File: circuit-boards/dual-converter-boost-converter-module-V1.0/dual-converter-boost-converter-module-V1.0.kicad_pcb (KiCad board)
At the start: 4 copper layers, 70 x 34 mm, 39 parts, among them J1 Vout Conn, J2 Conn_01x06, J3 Vout Conn, U1 TPL0401B-10DCKR, U2 LM5156HPWPR, U3 STN3N40K3

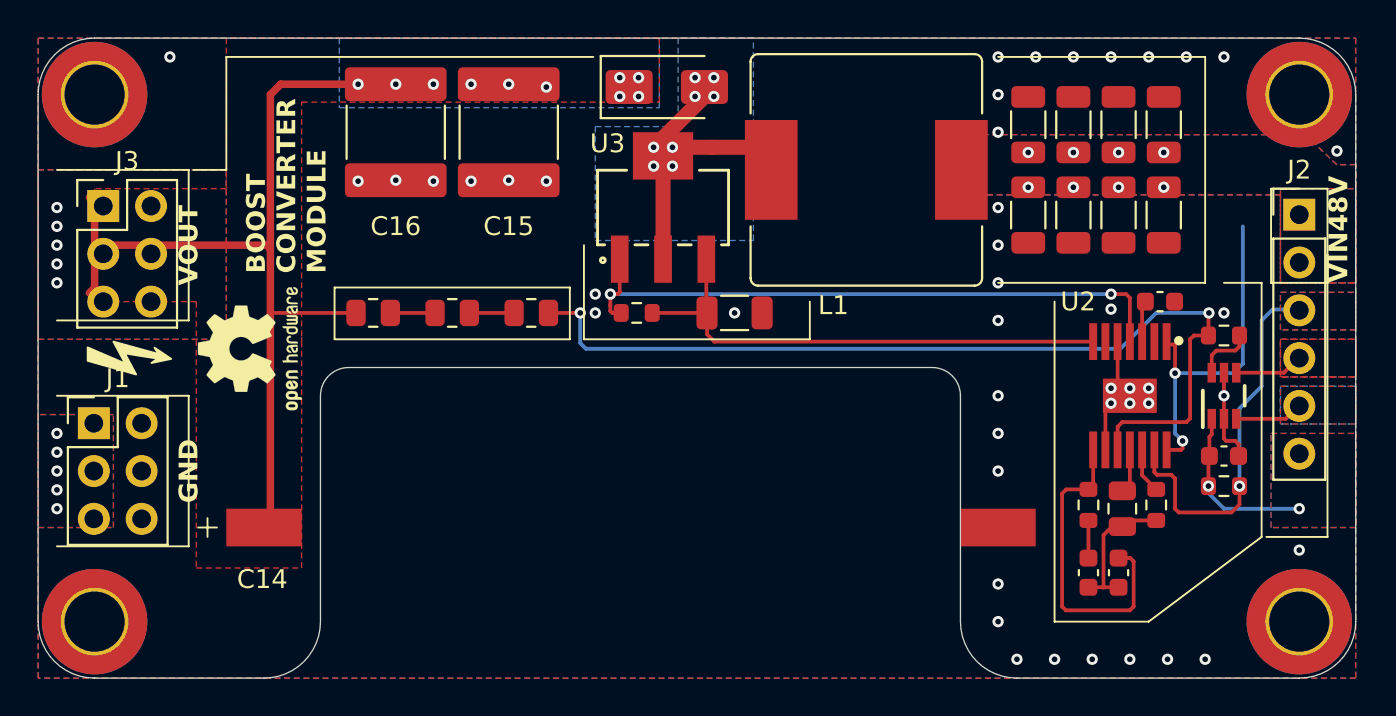
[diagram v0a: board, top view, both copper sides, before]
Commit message: align and lock connectors and mountpoints. improve track sizing and layout
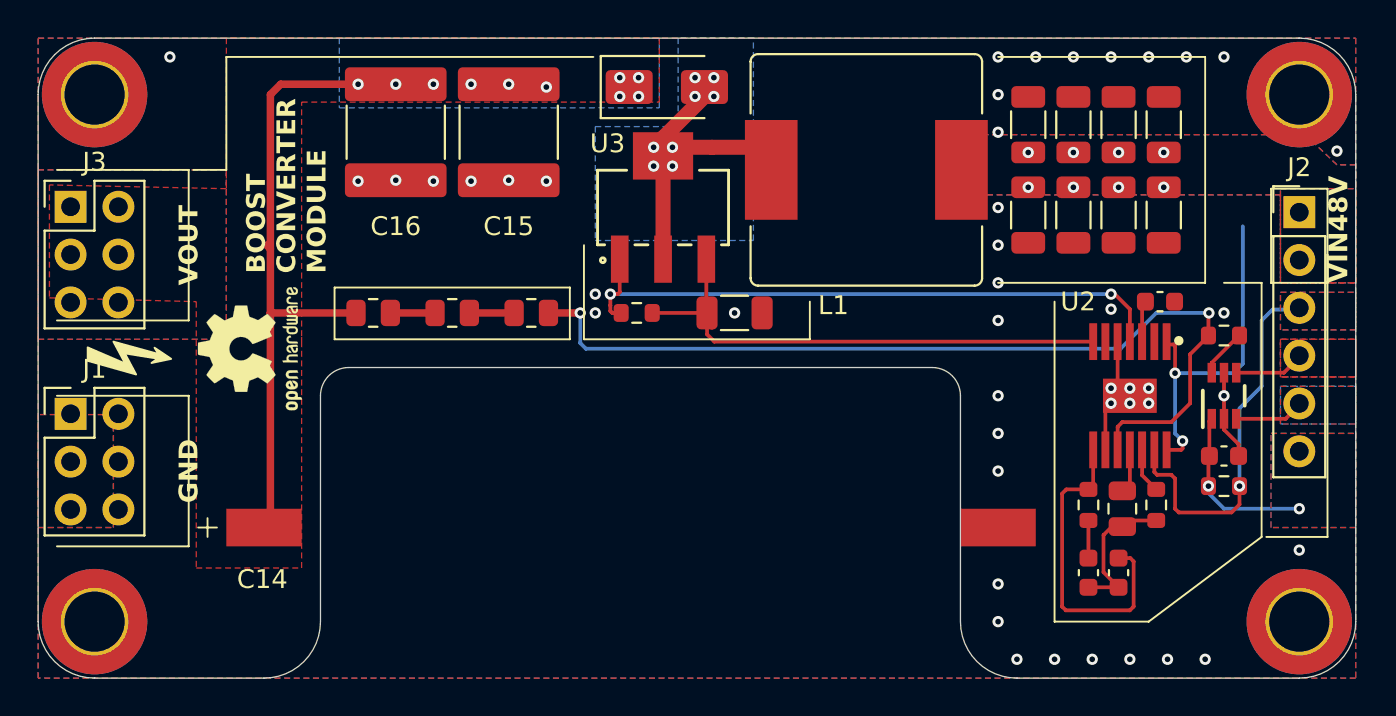
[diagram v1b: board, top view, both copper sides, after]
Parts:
- moved J3 1.74 mm to (38.7, 46.0)
- moved J1 1.33 mm to (38.7, 57.0)
- moved J2 0.13 mm to (104.0, 46.2)
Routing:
- net /COUT_BOOST: track 55.0 -> 40.6 mm, vias 15 -> 10
- net /V_FEEDBACK: track 49.3 -> 48.4 mm
- net Net-(U1-H): track 3.17 -> 2.60 mm
- net GND: vias 50 -> 45
